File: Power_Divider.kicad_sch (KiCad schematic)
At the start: 28 parts, among them J8 Molex 73251-1153, J9 2118714-2, P10 CONUFL001-SMD-T, P11 CONUFL001-SMD-T, P12 CONUFL001-SMD-T, P9 CONUFL001-SMD-T, U25 QPL9547, U26 RBP-140+

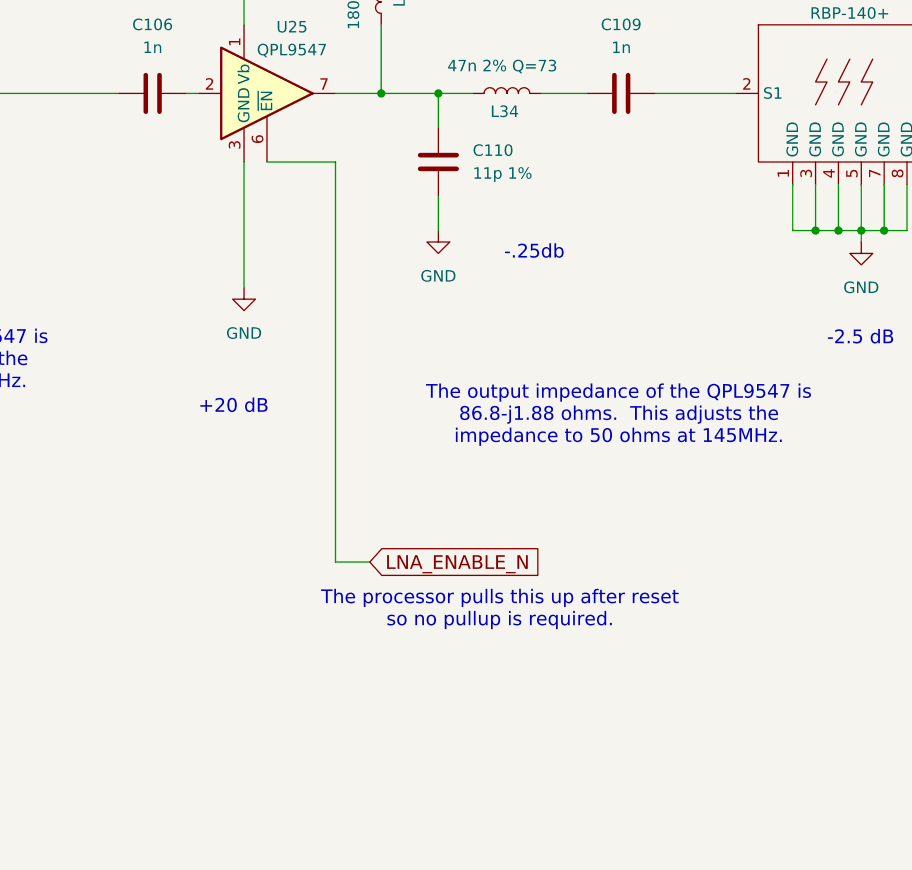
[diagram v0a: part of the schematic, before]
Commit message: More notes, added a pullup on LNA_ENABLE_N
Signed-off-by: Corey Minyard <corey@minyard.net>
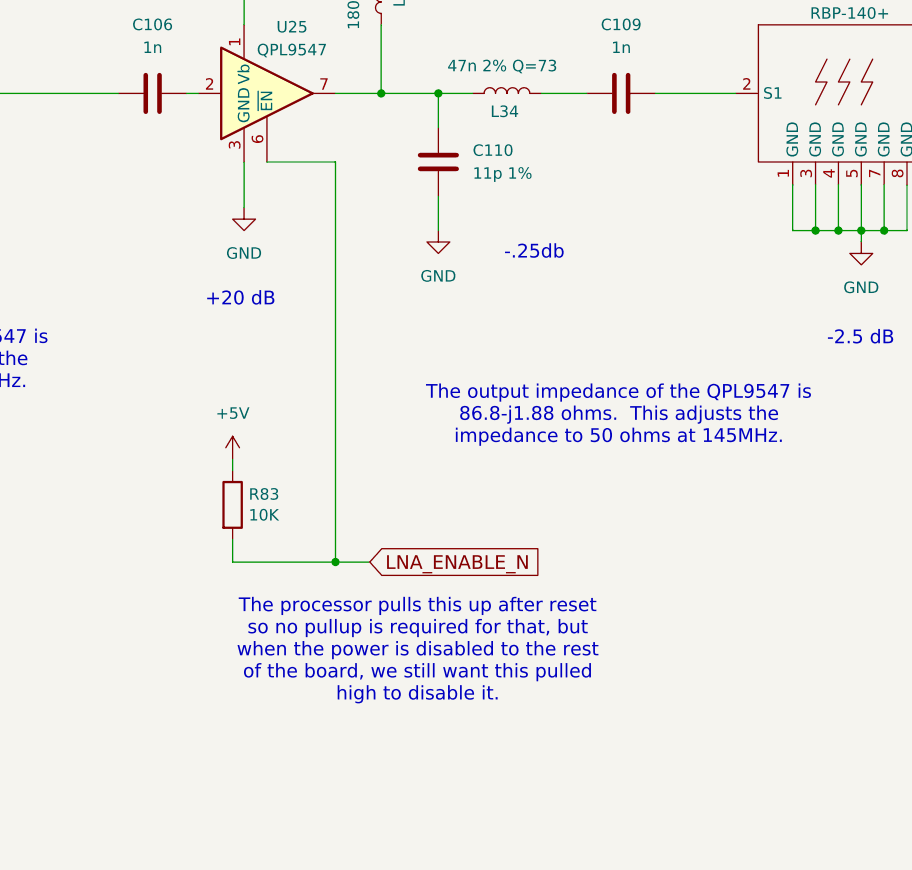
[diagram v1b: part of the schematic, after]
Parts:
- added R83: 10K, Resistor_SMD:R_0603_1608Metric_Pad0.98x0.95mm_HandSolder, symbol Device:R
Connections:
- net +5V: now also R83.1
- net LNA_ENABLE_N: now also R83.2
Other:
- note added: "The processor pulls this up after reset so no pullup is required for that, but when the power is disabled to the rest of the board, we still want this pulled high to disable it."
- note removed: "The processor pulls this up after reset so no pullup is required."
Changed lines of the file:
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@@
 		)
 	)
-	(text "The processor pulls this up after reset\nso no pullup is required."
+	(text "The processor pulls this up after reset\nso no pullup is required for that, but\nwhen the power is disabled to the rest\nof the board, we still want this pulled\nhigh to disable it."
 		(exclude_from_sim no)
-		(at 210.058 200.914 0)
+		(at 200.914 205.486 0)
 		(effects
 			(font
@@
 	(text "+20 dB"
 		(exclude_from_sim no)
-		(at 176.53 179.324 0)
+		(at 177.292 167.386 0)
 		(effects
 			(font
@@
 	)
 	(junction
+		(at 191.77 195.58)
+		(diameter 0)
+		(color 0 0 0 0)
+	)
+	(junction
 		(at 347.98 133.35)
 		(diameter 0)
@@
 	(wire
 		(pts
+			(xy 191.77 151.13) (xy 191.77 195.58)
+		)
+		(stroke
+			(width 0)
+			(type default)
+		)
+	)
+	(wire
+		(pts
+			(xy 180.34 184.15) (xy 180.34 185.42)
+		)
+		(stroke
+			(width 0)
+			(type default)
+		)
+	)
+	(wire
+		(pts
 			(xy 196.85 121.92) (xy 196.85 110.49)
 		)
@@
 	(wire
 		(pts
-			(xy 181.61 151.13) (xy 181.61 165.1)
+			(xy 181.61 151.13) (xy 181.61 156.21)
 		)
 		(stroke
@@
 	(wire
 		(pts
+			(xy 180.34 195.58) (xy 180.34 193.04)
+		)
+		(stroke
+			(width 0)
+			(type default)
+		)
+	)
+	(wire
+		(pts
 			(xy 342.9 114.3) (xy 342.9 123.19)
 		)
@@
 	(wire
 		(pts
-			(xy 191.77 151.13) (xy 191.77 195.58)
+			(xy 247.65 153.67) (xy 247.65 158.75)
 		)
 		(stroke
@@
 	(wire
 		(pts
-			(xy 247.65 153.67) (xy 247.65 158.75)
+			(xy 368.3 133.35) (xy 368.3 134.62)
 		)
 		(stroke
@@
 	(wire
 		(pts
-			(xy 368.3 133.35) (xy 368.3 134.62)
+			(xy 180.34 195.58) (xy 191.77 195.58)
 		)
 		(stroke
@@
 	)
 	(symbol
+		(lib_id "power:+5V")
+		(at 180.34 184.15 0)
+		(unit 1)
+		(exclude_from_sim no)
+		(in_bom yes)
+		(on_board yes)
+		(dnp no)
+		(fields_autoplaced yes)
+		(property "Reference" "#PWR0246"
+			(at 180.34 187.96 0)
+			(effects
+				(font
+					(size 1.27 1.27)
+				)
+				(hide yes)
+			)
+		)
+		(property "Value" "+5V"
+			(at 180.34 179.07 0)
+			(effects
+				(font
+					(size 1.27 1.27)
+				)
+			)
+		)
+		(property "Footprint" ""
+			(at 180.34 184.15 0)
+			(effects
+				(font
+					(size 1.27 1.27)
+				)
+				(hide yes)
+			)
+		)
+		(property "Datasheet" ""
+			(at 180.34 184.15 0)
+			(effects
+				(font
+					(size 1.27 1.27)
+				)
+				(hide yes)
+			)
+		)
+		(property "Description" ""
+			(at 180.34 184.15 0)
+			(effects
+				(font
+					(size 1.27 1.27)
+				)
+			)
+		)
+		(pin "1"
+		)
+		(instances
+			(project "PacSat_AFSK"
+				(path "/cc9f42d2-6985-41ac-acab-5ab7b01c5b38/9af0eacb-5211-4e23-85d7-9c1805bbe6a4"
+					(reference "#PWR0246")
+					(unit 1)
+				)
+			)
+		)
+	)
+	(symbol
 		(lib_id "Device:L")
 		(at 210.82 143.51 270)
@@
 	)
 	(symbol
+		(lib_id "Device:R")
+		(at 180.34 189.23 0)
+		(unit 1)
+		(exclude_from_sim no)
+		(in_bom yes)
+		(on_board yes)
+		(dnp no)
+		(property "Reference" "R83"
+			(at 182.118 188.0616 0)
+			(effects
+				(font
+					(size 1.27 1.27)
+				)
+				(justify left)
+			)
+		)
+		(property "Value" "10K"
+			(at 182.118 190.373 0)
+			(effects
+				(font
+					(size 1.27 1.27)
+				)
+				(justify left)
+			)
+		)
+		(property "Footprint" "Resistor_SMD:R_0603_1608Metric_Pad0.98x0.95mm_HandSolder"
+			(at 178.562 189.23 90)
+			(effects
+				(font
+					(size 1.27 1.27)
+				)
+				(hide yes)
+			)
+		)
+		(property "Datasheet" "~"
+			(at 180.34 189.23 0)
+			(effects
+				(font
+					(size 1.27 1.27)
+				)
+				(hide yes)
+			)
+		)
+		(property "Description" ""
+			(at 180.34 189.23 0)
+			(effects
+				(font
+					(size 1.27 1.27)
+				)
+			)
+		)
+		(pin "1"
+		)
+		(pin "2"
+		)
+		(instances
+			(project "PacSat_AFSK"
+				(path "/cc9f42d2-6985-41ac-acab-5ab7b01c5b38/9af0eacb-5211-4e23-85d7-9c1805bbe6a4"
+					(reference "R83")
+					(unit 1)
+				)
+			)
+		)
+	)
+	(symbol
 		(lib_id "PACSAT_DEV_misc:U_FL")
 		(at 349.25 123.19 0)
@@
 	(symbol
 		(lib_id "power:GND")
-		(at 181.61 165.1 0)
+		(at 181.61 156.21 0)
 		(unit 1)
 		(exclude_from_sim no)
@@
 		(fields_autoplaced yes)
 		(property "Reference" "#PWR0209"
-			(at 181.61 171.45 0)
+			(at 181.61 162.56 0)
 			(effects
 				(font
@@
 		)
 		(property "Value" "GND"
-			(at 181.61 170.18 0)
+			(at 181.61 161.29 0)
 			(effects
 				(font
@@
 		)
 		(property "Footprint" ""
-			(at 181.61 165.1 0)
+			(at 181.61 156.21 0)
 			(effects
 				(font
@@
 		)
 		(property "Datasheet" ""
-			(at 181.61 165.1 0)
+			(at 181.61 156.21 0)
 			(effects
 				(font
@@
 		)
 		(property "Description" ""
-			(at 181.61 165.1 0)
+			(at 181.61 156.21 0)
 			(effects
 				(font

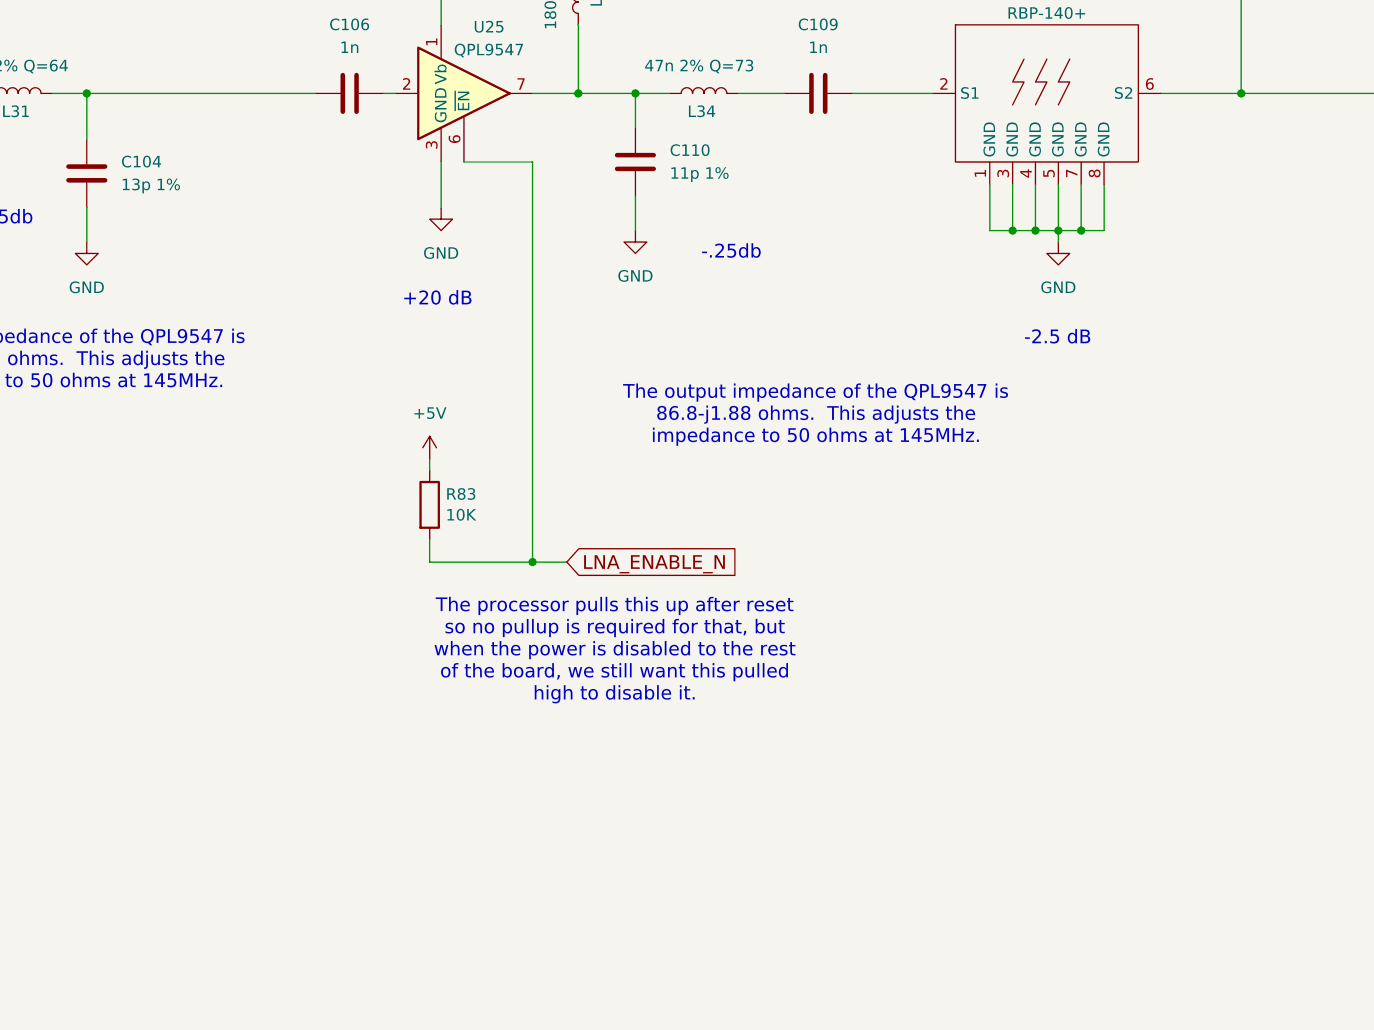
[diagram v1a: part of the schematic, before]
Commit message: Rework the LNA enable line
Don't connect +5V through a pullup to a GPIO.  That's not in spec
for the GPIO lines.

Signed-off-by: Corey Minyard <corey@minyard.net>
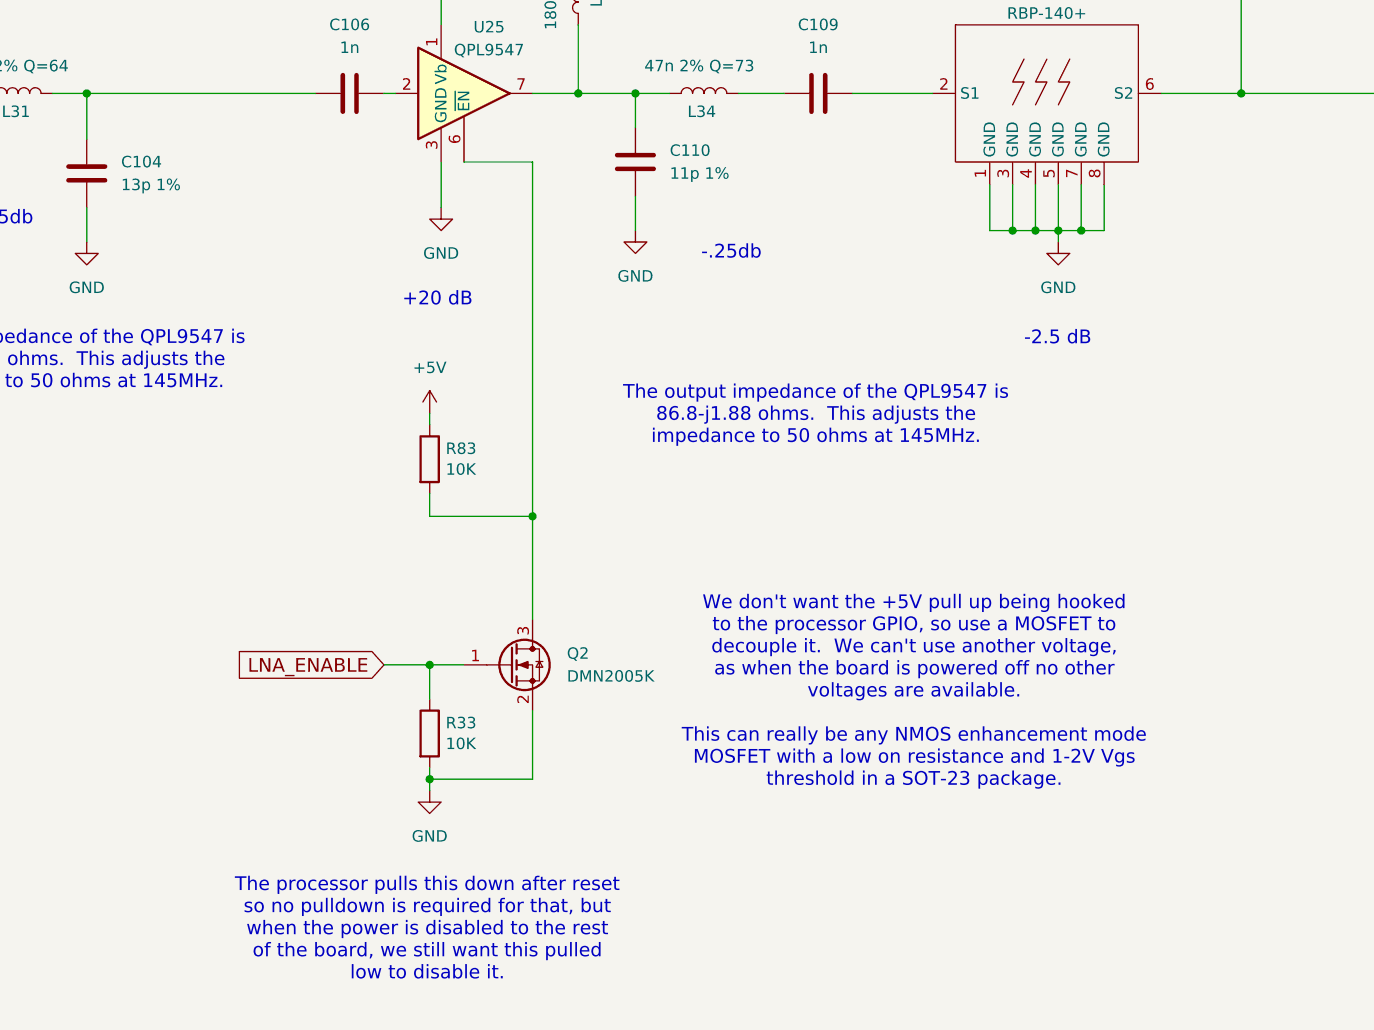
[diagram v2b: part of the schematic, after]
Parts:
- added Q2: DMN2005K, Package_TO_SOT_SMD:SOT-23_Handsoldering, symbol Transistor_FET:Q_NMOS_GSD
- added R33: 10K, Resistor_SMD:R_0603_1608Metric_Pad0.98x0.95mm_HandSolder, symbol Device:R
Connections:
- net GND: now also Q2.2 (S), R33.2
- net LNA_ENABLE_N: no longer names the net of R83.2, U25.6 (~{EN})
- net LNA_ENABLE_N: now also Q2.3 (D)
- new net LNA_ENABLE: Q2.1 (G), R33.1
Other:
- note added: "The processor pulls this down after reset so no pulldown is required for that, but when the power is disabled to the rest of the board, we still want this pulled low to disable it."
- note added: "We don't want the +5V pull up being hooked to the processor GPIO, so use a MOSFET to decouple it. We can't use another voltage, as when the board is powered off no other voltages are available. This can really be any NMOS enhancement mode MOSFET with a low on resistance and 1-2V Vgs threshold in a SOT-23 package."
- note removed: "The processor pulls this up after reset so no pullup is required for that, but when the power is disabled to the rest of the board, we still want this pulled high to disable it."
- moved on the sheet: R83

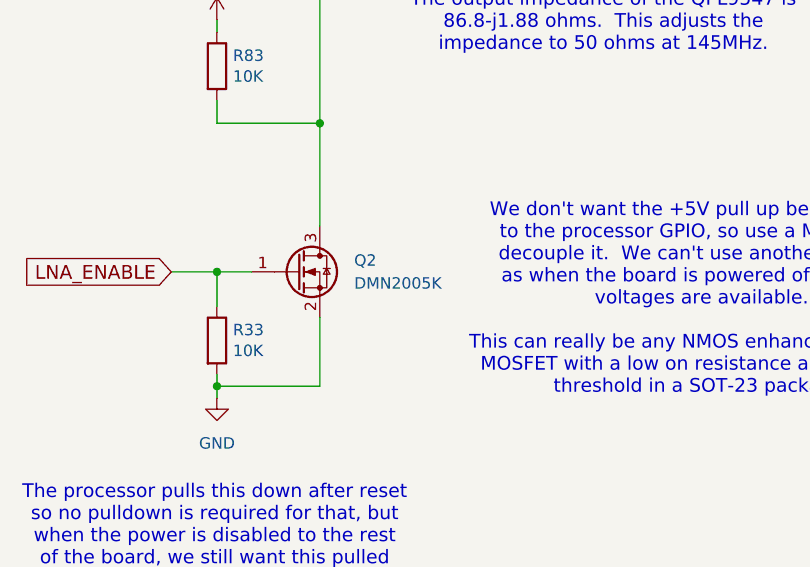
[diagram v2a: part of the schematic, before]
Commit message: Notes cleanups, replace LNA enable MOSFET with BSS138
Signed-off-by: Corey Minyard <corey@minyard.net>
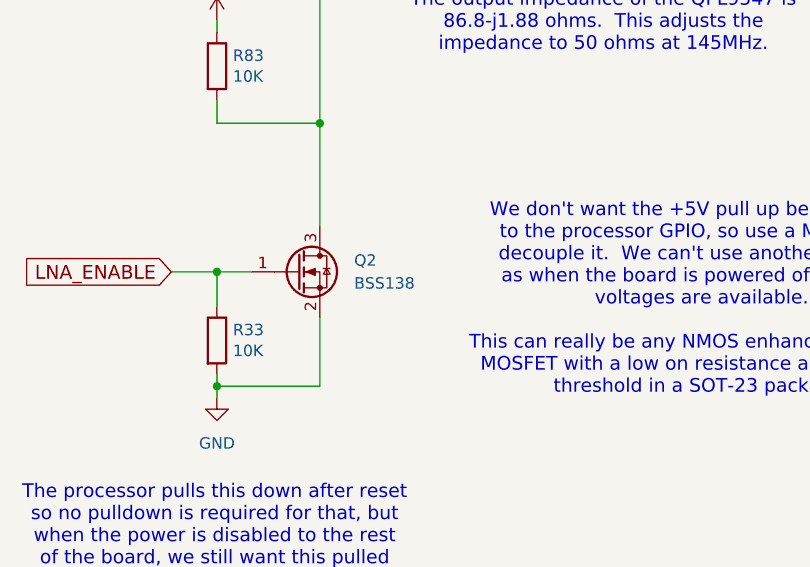
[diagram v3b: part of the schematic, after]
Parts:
- Q2: value DMN2005K -> BSS138; footprint Package_TO_SOT_SMD:SOT-23_Handsoldering -> Package_TO_SOT_SMD:SOT-23
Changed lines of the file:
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@@
 			)
 		)
-		(property "Value" "DMN2005K"
+		(property "Value" "BSS138"
 			(at 195.58 208.2799 0)
 			(effects
@@
 			)
 		)
-		(property "Footprint" "Package_TO_SOT_SMD:SOT-23_Handsoldering"
+		(property "Footprint" "Package_TO_SOT_SMD:SOT-23"
 			(at 194.31 204.47 0)
 			(effects

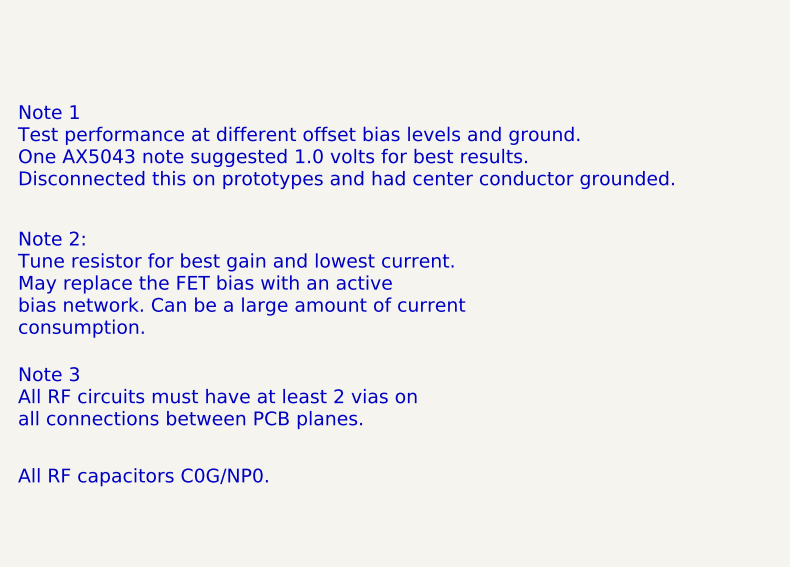
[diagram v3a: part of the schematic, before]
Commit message: Check over notes and some component values
Fix a wrong capacitor in one spot, set Q and voltage as necessary.

Signed-off-by: Corey Minyard <corey@minyard.net>
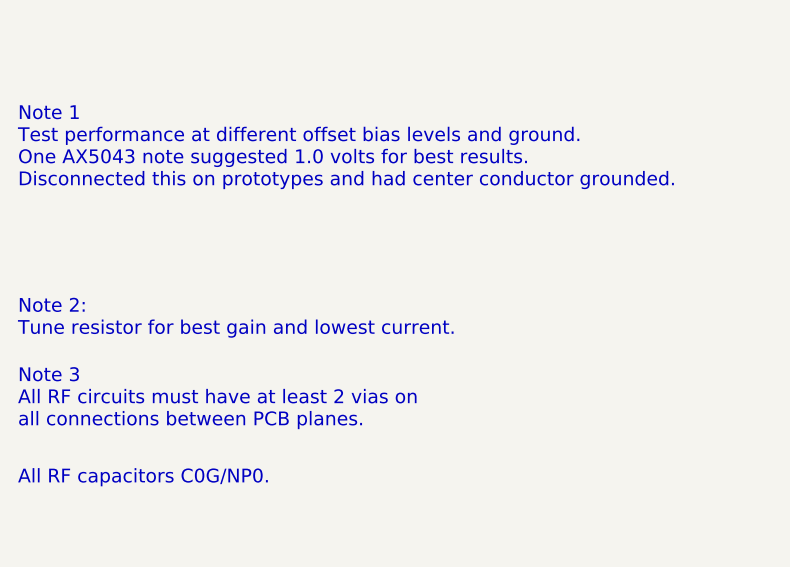
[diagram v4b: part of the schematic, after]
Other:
- note added: "Note 2: Tune resistor for best gain and lowest current."
- note removed: "Note 2: Tune resistor for best gain and lowest current. May replace the FET bias with an active bias network. Can be a large amount of current consumption."
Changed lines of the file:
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@@
 		)
 	)
-	(text "Note 2:\nTune resistor for best gain and lowest current.\nMay replace the FET bias with an active \nbias network. Can be a large amount of current\nconsumption."
+	(text "Note 2:\nTune resistor for best gain and lowest current."
 		(exclude_from_sim no)
 		(at 27.94 218.44 0)
